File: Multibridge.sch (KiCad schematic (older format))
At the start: 2 parts

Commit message: Upgrade FPGA size, re-route SDRAM
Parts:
- removed BRIDGE1: XC6SLX25-CSG324, manuf:XILINX-CSG324, symbol XC6SLX25-CSG324
- added BRIDGE1: XC6SLX25-FGG484, manuf:XILINX-FGG484, symbol XC6SLX25-FGG484
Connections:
- net labels added: VCCO1, VDDRREF, VRAM
- net labels removed: CD0, CD1, CD10, CD11, CD12, CD13, CD14, CD15, CD16, CD17, CD18, CD19, CD2, CD20, CD21, CD22, CD23, CD24, CD25, CD26, CD27, CD28, CD29, CD3, CD30, CD31, CD4, CD5, CD6, CD7, CD8, CD9, CD[0..31], CD_CLK, CD_MISO, CD_MOSI, CD_R/~W, CD_SCLK, CD_~ADH, CD_~ADL, CD_~SS0, CD_~SS1, CD_~SS2, CD_~SS3, CD_~SS4, CD_~SS5, CD_~SS[0..5], CPU0, CPU1, CPU10, CPU11, CPU12, CPU13, CPU14, CPU15, CPU2, CPU3, CPU4, CPU5, CPU6, CPU7, CPU8, CPU9, CPUASTR, CPUCLK, CPUDSTR, CPU[0..15], CPUnW, VREF, ~SS[0..5]
- wire segments 327 -> 301
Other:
- note removed: "CPU interface:\n64 bit data, sent 16 bits at a time at max speed\n\nAddress packet:\n64 bit packet, MSB high for autoincrement mode\nCPUASTR (address strobe) low with first bit to synchronize\nCPUnW - assert during the final bit of address packet to\n indicate data will be written, not read\n\nData packet:\n64 bit packet\nCPUDSTR (data strobe) low with first bit to synchronize\nCan transmit multi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"
- moved on the sheet: SODIMM1A

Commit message: MOAR WORK, v2
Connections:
- net labels added: /PerBus/PCI_AD0, /PerBus/PCI_AD1, /PerBus/PCI_AD10, /PerBus/PCI_AD11, /PerBus/PCI_AD12, /PerBus/PCI_AD13, /PerBus/PCI_AD14, /PerBus/PCI_AD15, /PerBus/PCI_AD16, /PerBus/PCI_AD17, /PerBus/PCI_AD18, /PerBus/PCI_AD19, /PerBus/PCI_AD2, /PerBus/PCI_AD20, /PerBus/PCI_AD21, /PerBus/PCI_AD22, /PerBus/PCI_AD23, /PerBus/PCI_AD24, /PerBus/PCI_AD25, /PerBus/PCI_AD26, /PerBus/PCI_AD27, /PerBus/PCI_AD28, /PerBus/PCI_AD29, /PerBus/PCI_AD3, /PerBus/PCI_AD30, /PerBus/PCI_AD31, /PerBus/PCI_AD4, /PerBus/PCI_AD5, /PerBus/PCI_AD6, /PerBus/PCI_AD7, /PerBus/PCI_AD8, /PerBus/PCI_AD9, /PerBus/PCI_CLK, /PerBus/PCI_GNT#0, /PerBus/PCI_GNT#1, /PerBus/PCI_GNT#2, /PerBus/PCI_GNT#3, /PerBus/PCI_INTA#, /PerBus/PCI_INTB#, /PerBus/PCI_INTC#, /PerBus/PCI_INTD#, /PerBus/PCI_REQ#0, /PerBus/PCI_REQ#1, /PerBus/PCI_REQ#2, /PerBus/PCI_REQ#3, LIMBA15, LIMBD0, LIMBD1, LIMBD2, LIMBD3, LIMBD4, LIMBD5, LIMBD6, LIMBD7, LIMBD[0..7], LIMBNCS, LIMBNRD, LIMBNWAIT, LIMBNWE, LIMBREQ, VCCO_2
- net labels removed: VCCO1
- wire segments 301 -> 368
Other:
- moved on the sheet: BRIDGE1B, BRIDGE1C, SODIMM1A

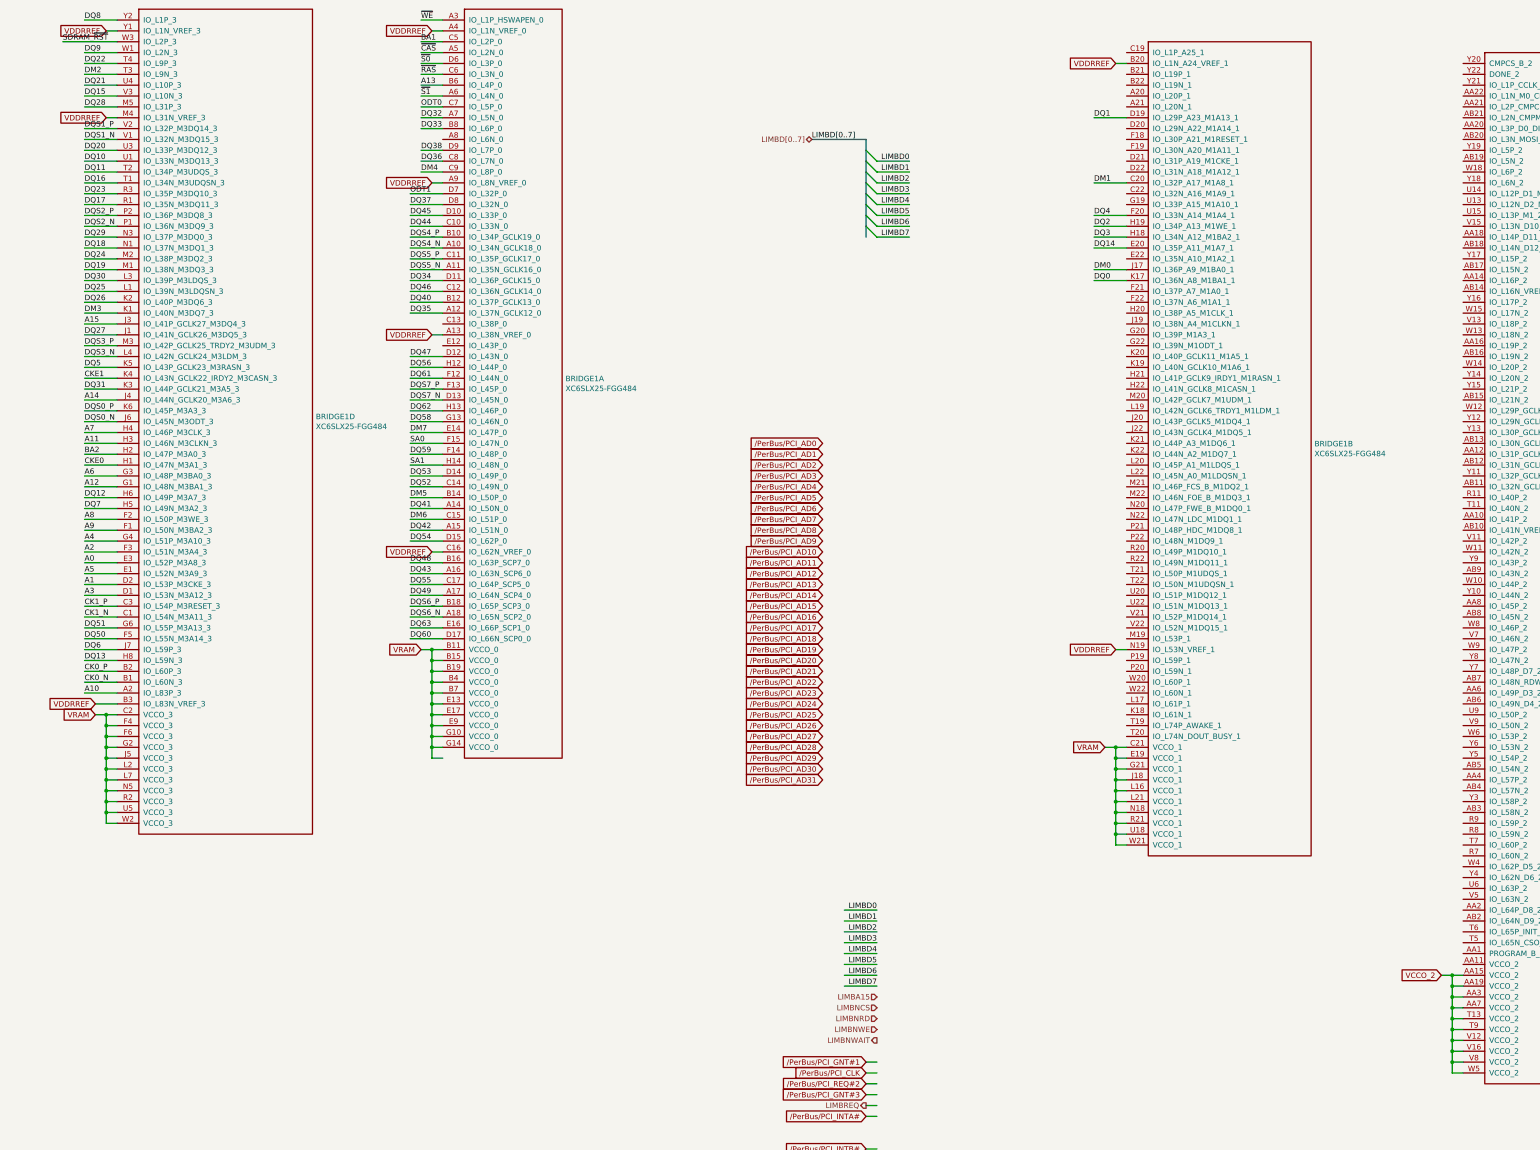
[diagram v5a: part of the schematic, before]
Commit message: Rip up SDRAM and rotate FPGA
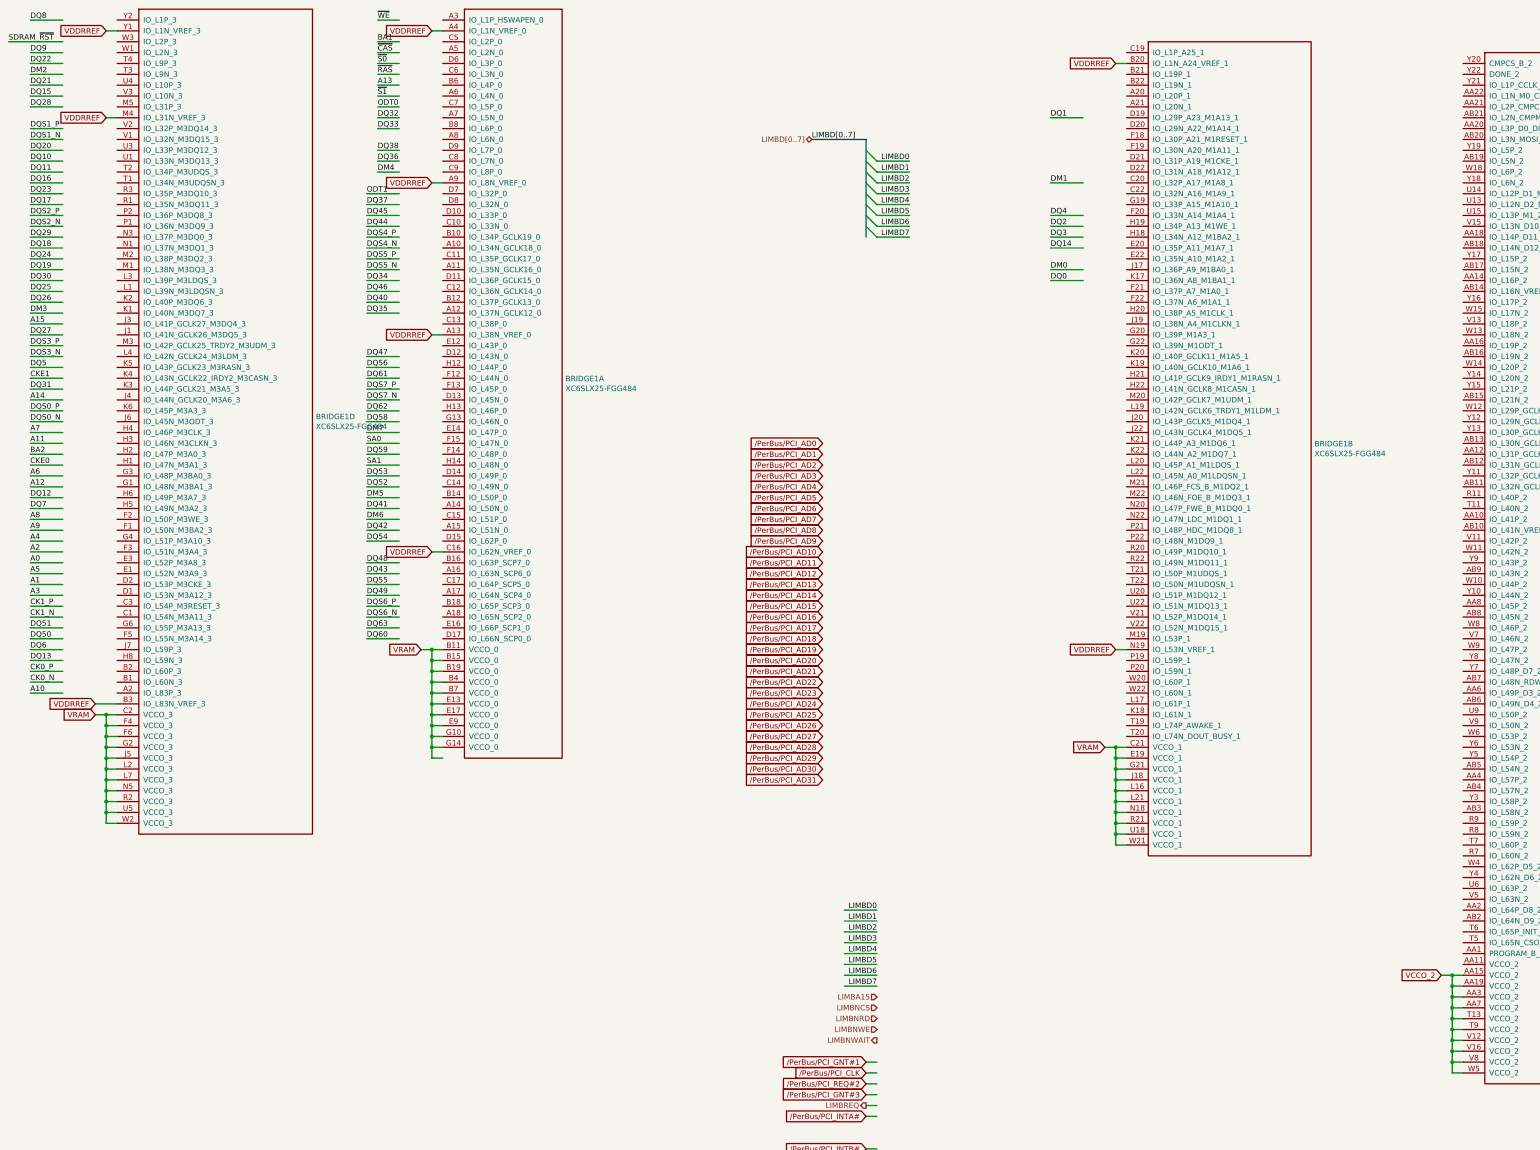
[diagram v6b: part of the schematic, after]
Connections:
- wire segments 368 -> 330

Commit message: Reroute SDRAM after bank swap
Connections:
- wire segments 330 -> 332

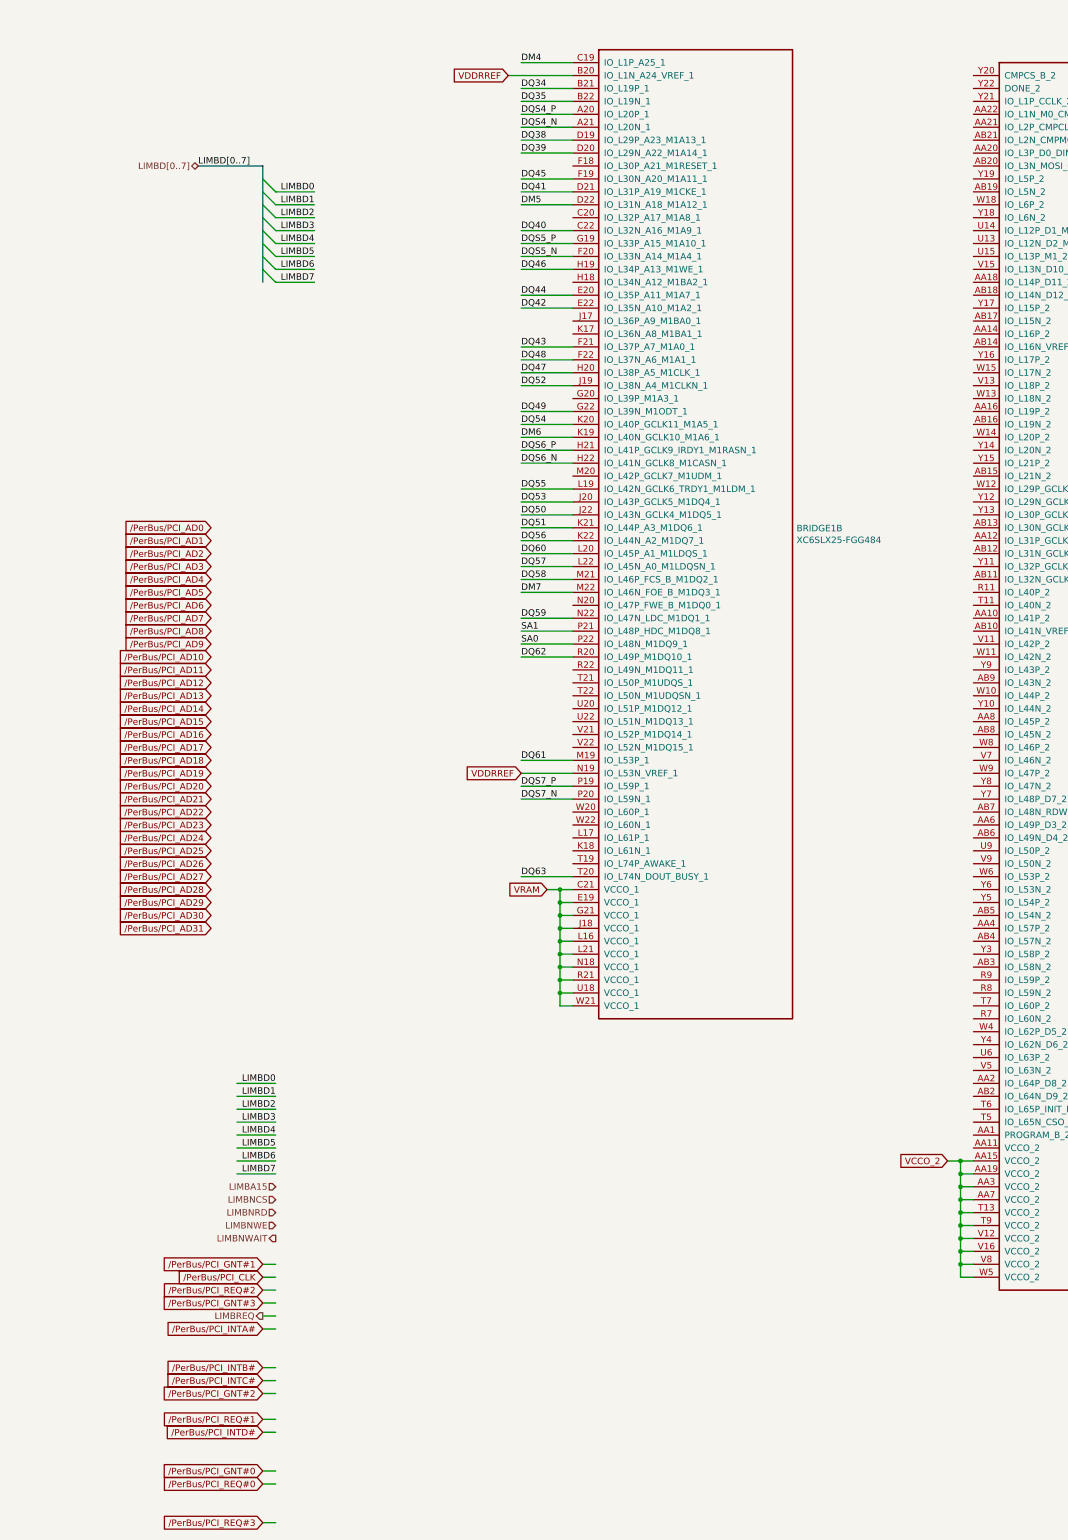
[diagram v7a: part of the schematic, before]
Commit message: Route EC and half of PCI bus to bridge
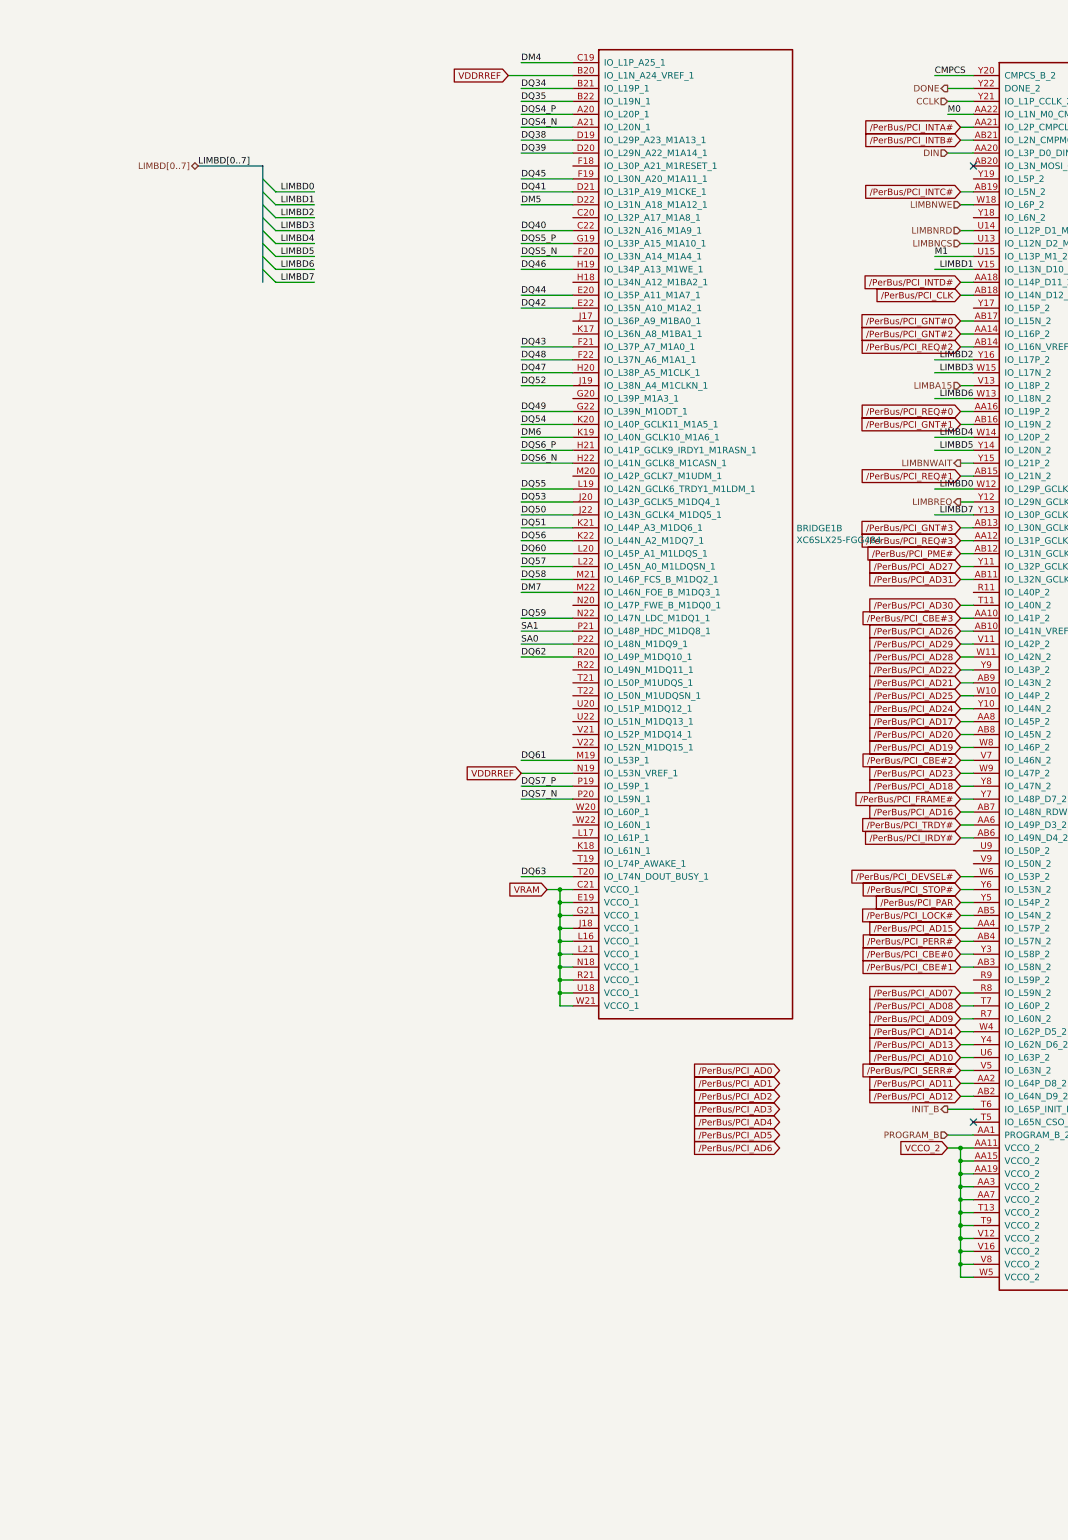
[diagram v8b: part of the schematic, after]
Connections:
- net labels added: /PerBus/PCI_AD07, /PerBus/PCI_AD08, /PerBus/PCI_AD09, /PerBus/PCI_CBE#0, /PerBus/PCI_CBE#1, /PerBus/PCI_CBE#2, /PerBus/PCI_CBE#3, /PerBus/PCI_DEVSEL#, /PerBus/PCI_FRAME#, /PerBus/PCI_IRDY#, /PerBus/PCI_LOCK#, /PerBus/PCI_PAR, /PerBus/PCI_PERR#, /PerBus/PCI_PME#, /PerBus/PCI_SERR#, /PerBus/PCI_STOP#, /PerBus/PCI_TRDY#, CCLK, CMPCS, DIN, DONE, INIT_B, M0, M1, PROGRAM_B
- net labels removed: /PerBus/PCI_AD7, /PerBus/PCI_AD8, /PerBus/PCI_AD9
- wire segments 332 -> 385
- no-connect marks 0 -> 2
